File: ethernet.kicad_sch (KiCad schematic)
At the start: 9 parts, among them U1 MX6UL-VM

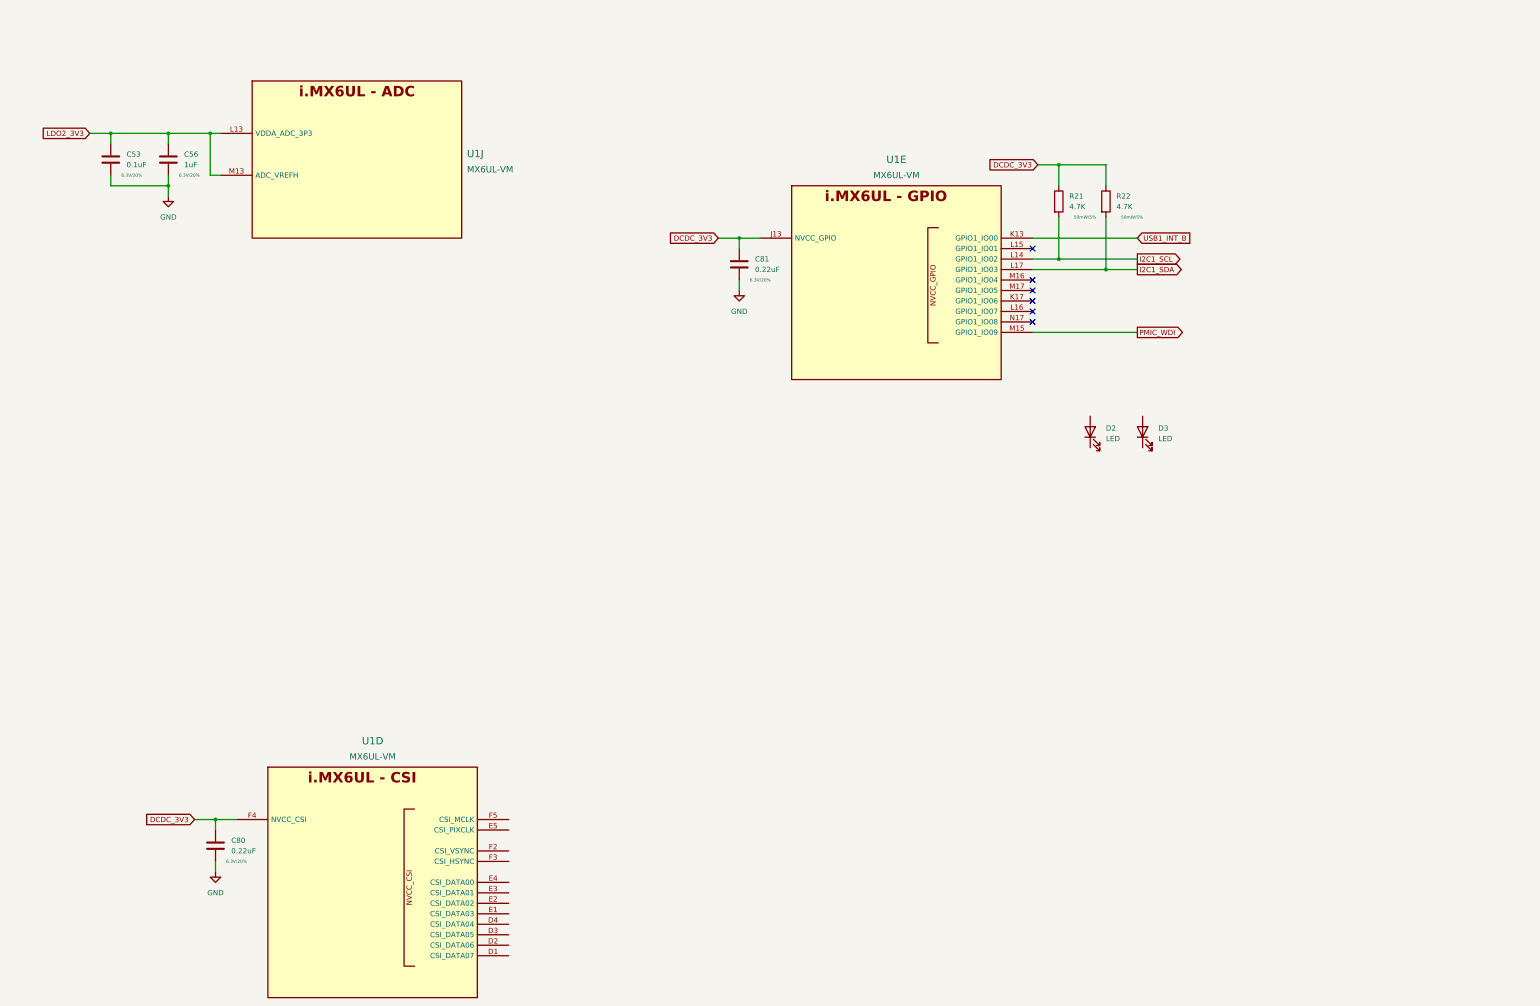
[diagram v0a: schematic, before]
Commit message: more ddr routing, add more connectors
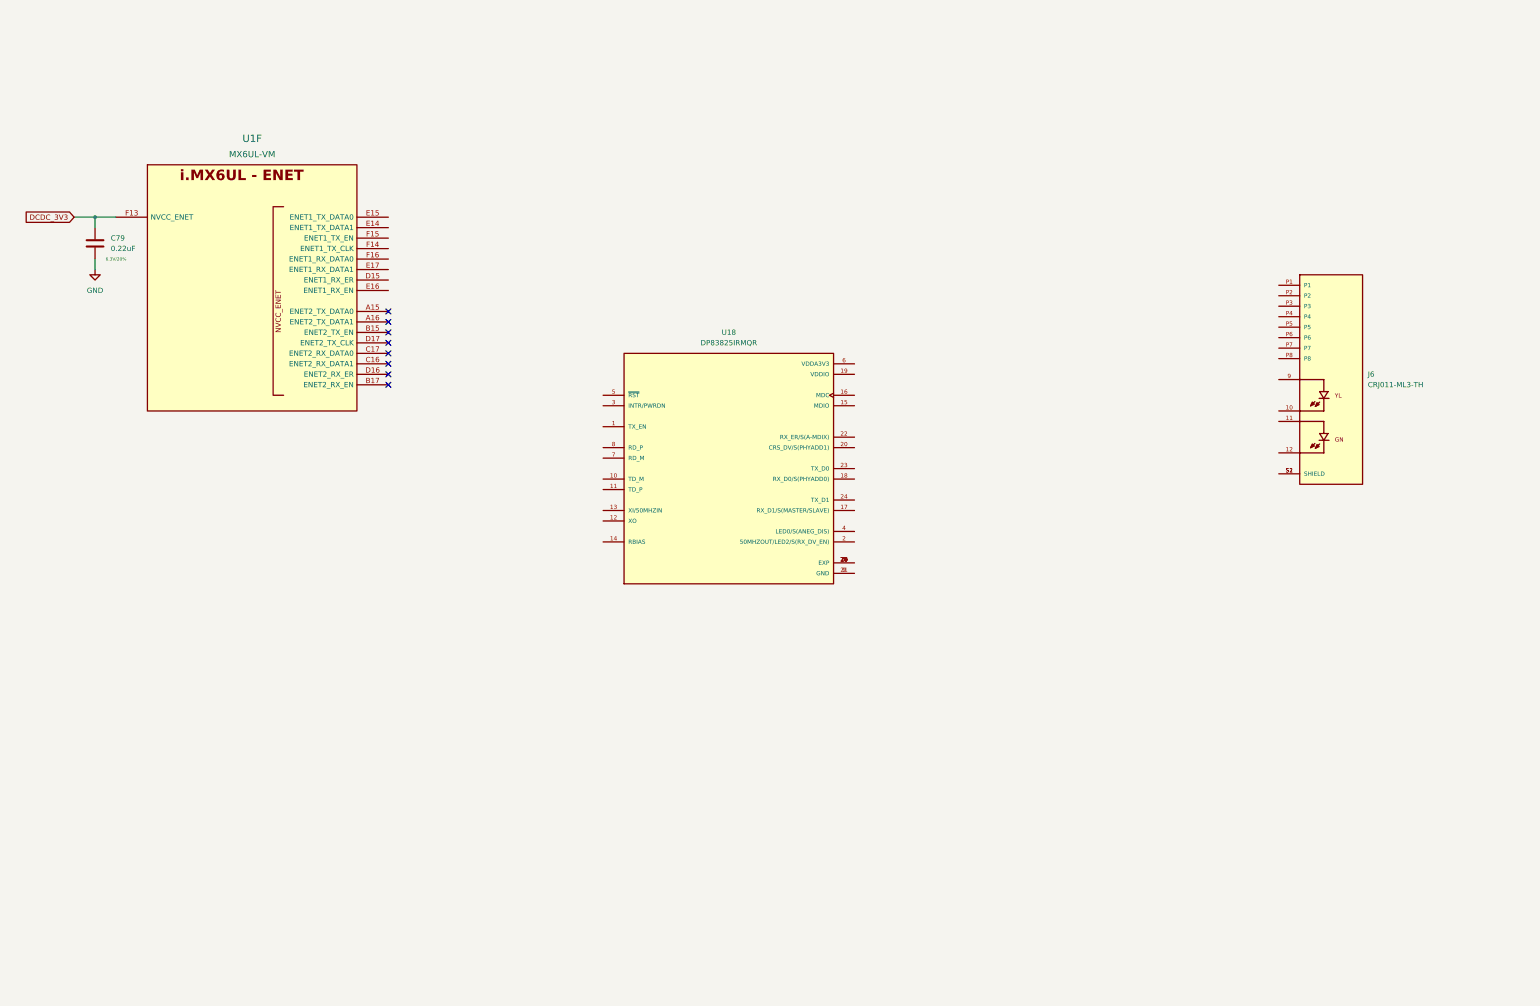
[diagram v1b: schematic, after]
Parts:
- removed C53: 0.1uF, Capacitor_SMD:C_0402_1005Metric, symbol Device:C
- removed C56: 1uF, Capacitor_SMD:C_0402_1005Metric, symbol Device:C
- removed C80, C81: 0.22uF, Capacitor_SMD:C_0402_1005Metric, symbol Device:C
- removed D2, D3: LED, LED_SMD:LED_0603_1608Metric, symbol Device:LED
- removed R21, R22: 4.7K, Resistor_SMD:R_0402_1005Metric, symbol Device:R
- removed U1: MX6UL-VM, imx6ull-sbc:SOT1534-2, symbol imx6ull-sbc:MX6UL-VM
- added C79: 0.22uF, Capacitor_SMD:C_0402_1005Metric, symbol Device:C
- added J6: CRJ011-ML3-TH, imx6ull-sbc:CUI_CRJ011-ML3-TH, symbol imx6ull-sbc:CRJ011-ML3-TH
- added U1: MX6UL-VM, imx6ull-sbc:SOT1534-2, symbol imx6ull-sbc:MX6UL-VM
- added U18: DP83825IRMQR, imx6ull-sbc:XCVR_DP83825IRMQR, symbol imx6ull-sbc:DP83825IRMQR
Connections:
- net DCDC_3V3: now also C79.1, U1.F13 (NVCC_ENET)
- net GND: now also C79.2
- new net: U18.21 (GND), U18.9 (GND)
- new net: U18.25 (EXP), U18.26 (EXP), U18.27 (EXP), U18.28 (EXP), U18.29 (EXP), U18.30 (EXP)
- new net: J6.S1 (SHIELD), J6.S2 (SHIELD)
- no-connect marks 6 -> 8

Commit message: move to hierarchal labels, work on power tree, add basic pcb layout
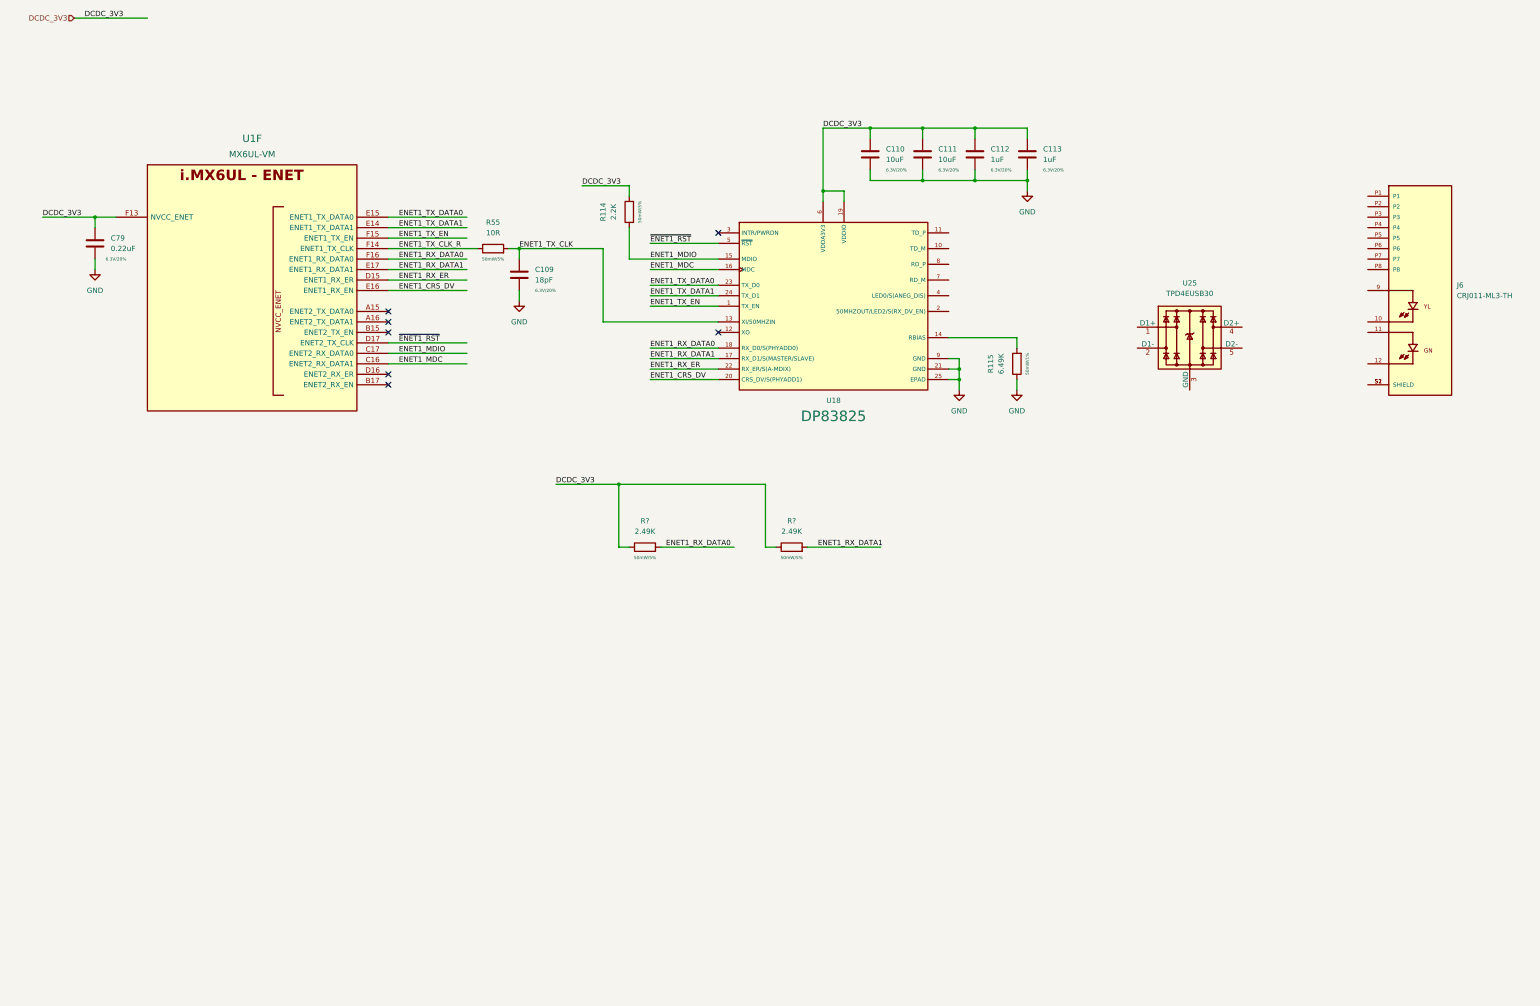
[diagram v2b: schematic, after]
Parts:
- removed U18: DP83825IRMQR, imx6ull-sbc:XCVR_DP83825IRMQR, symbol imx6ull-sbc:DP83825IRMQR
- added C109: 18pF, Capacitor_SMD:C_0402_1005Metric, symbol Device:C
- added C110, C111: 10uF, Capacitor_SMD:C_0402_1005Metric, symbol Device:C
- added C112, C113: 1uF, Capacitor_SMD:C_0402_1005Metric, symbol Device:C
- added R114: 2.2K, Resistor_SMD:R_0402_1005Metric, symbol Device:R
- added R115: 6.49K, Resistor_SMD:R_0402_1005Metric, symbol Device:R
- added R55: 10R, Resistor_SMD:R_0402_1005Metric, symbol Device:R
- added R? (x2): 2.49K, Resistor_SMD:R_0402_1005Metric, symbol Device:R
- added U18: DP83825, imx6ull-sbc:XCVR_DP83825IRMQR, symbol imx6ull-sbc:DP83825
- added U25: TPD4EUSB30, Package_SON:USON-10_2.5x1.0mm_P0.5mm, symbol imx6ull-sbc:TPD4EUSB30
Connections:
- net DCDC_3V3: now also C110.1, C111.1, C112.1, C113.1, R114.2, R?.1, R?.1, U18.19 (VDDIO), U18.6 (VDDA3V3)
- net GND: now also C109.2, C110.2, C111.2, C112.2, C113.2, R115.1, U18.21 (GND), U18.25 (EPAD), U18.9 (GND)
- net ENET1_MDC: now reaches U1.C16 (ENET2_RX_DATA1)
- net ENET1_MDC: now also U18.16 (MDC)
- net ENET1_MDIO: now reaches U1.C17 (ENET2_RX_DATA0)
- net ENET1_MDIO: now also R114.1, U18.15 (MDIO)
- net ENET1_RX_ER: now reaches U1.D15 (ENET1_RX_ER)
- net ENET1_RX_ER: now also U18.22 (RX_ER/S(A-MDIX))
- net ~{ENET1_RST}: now reaches U1.D17 (ENET2_TX_CLK)
- net ~{ENET1_RST}: now also U18.5 (~{RST})
- net ENET1_TX_DATA1: now reaches U1.E14 (ENET1_TX_DATA1)
- net ENET1_TX_DATA1: now also U18.24 (TX_D1)
- net ENET1_TX_DATA0: now reaches U1.E15 (ENET1_TX_DATA0)
- net ENET1_TX_DATA0: now also U18.23 (TX_D0)
- net ENET1_CRS_DV: now reaches U1.E16 (ENET1_RX_EN)
- net ENET1_CRS_DV: now also U18.20 (CRS_DV/S(PHYADD1))
- net ENET1_RX_DATA1: now reaches U1.E17 (ENET1_RX_DATA1)
- net ENET1_RX_DATA1: now also R?.2, U18.17 (RX_D1/S(MASTER/SLAVE))
- net ENET1_TX_CLK_R: now reaches U1.F14 (ENET1_TX_CLK)
- net ENET1_TX_CLK_R: now also R55.1
- net ENET1_TX_EN: now reaches U1.F15 (ENET1_TX_EN)
- net ENET1_TX_EN: now also U18.1 (TX_EN)
- net ENET1_RX_DATA0: now reaches U1.F16 (ENET1_RX_DATA0)
- net ENET1_RX_DATA0: now also R?.2, U18.18 (RX_D0/S(PHYADD0))
- new net: R115.2, U18.14 (RBIAS)
- new net: U25.1 (D1+), U25.10
- new net: U25.2 (D1-), U25.9
- new net: U25.3 (GND), U25.8 (GND)
- new net: U25.4 (D2+), U25.7
- new net: U25.5 (D2-), U25.6
- new net ENET1_TX_CLK: C109.1, R55.2, U18.13 (XI/50MHZIN)
- no-connect marks 8 -> 7
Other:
- moved on the sheet: J6

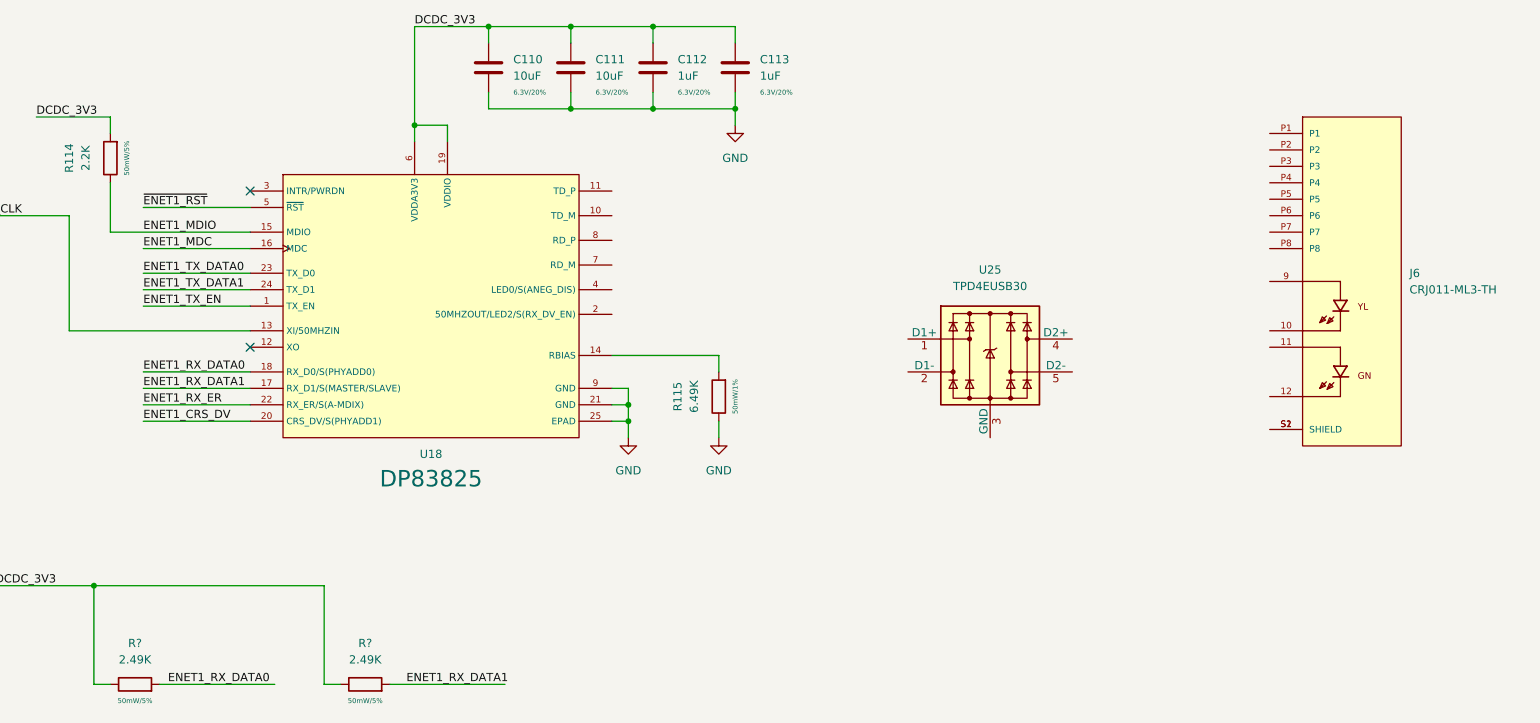
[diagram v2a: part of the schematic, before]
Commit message: most of sch done, inital component pcb placement
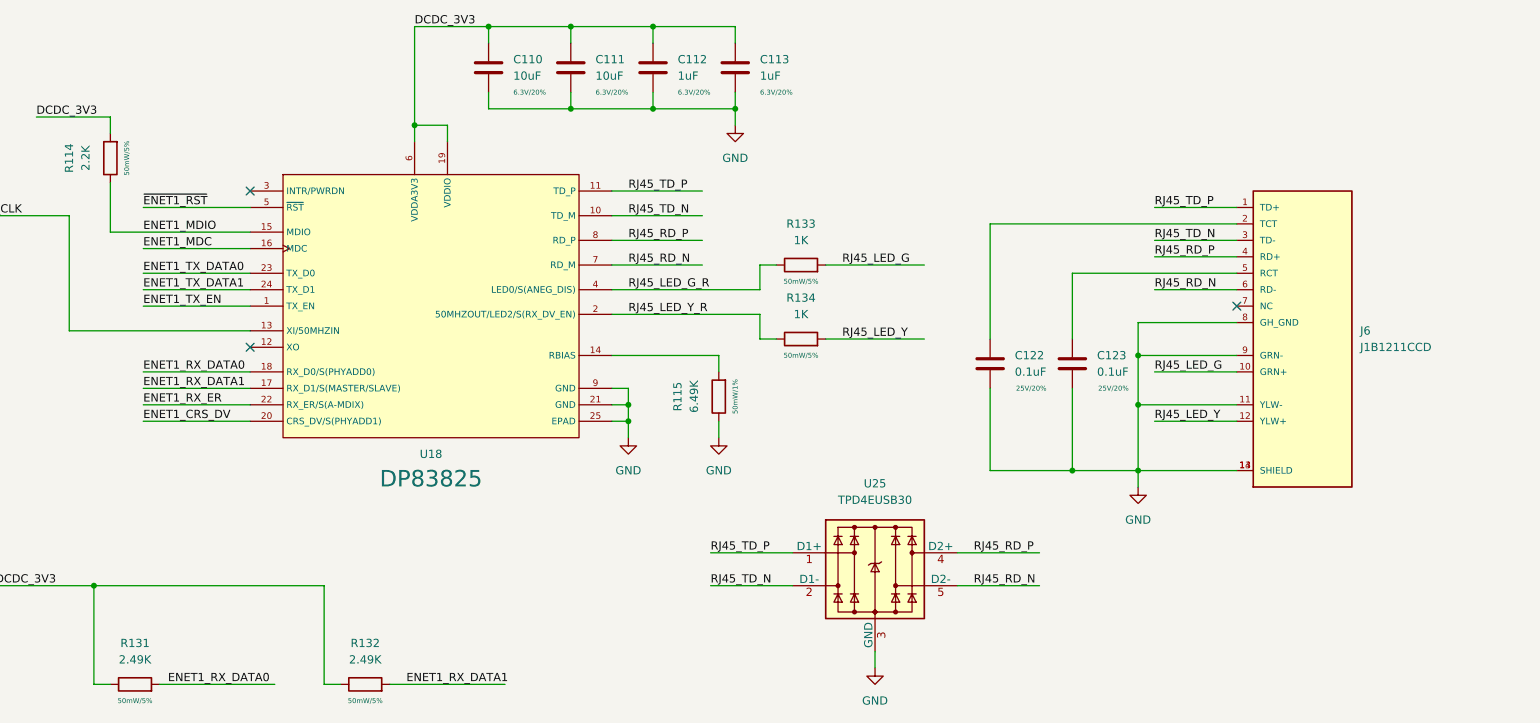
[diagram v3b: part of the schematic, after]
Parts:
- removed J6: CRJ011-ML3-TH, imx6ull-sbc:CUI_CRJ011-ML3-TH, symbol imx6ull-sbc:CRJ011-ML3-TH
- added C122, C123: 0.1uF, Capacitor_SMD:C_0402_1005Metric, symbol Device:C
- added J6: J1B1211CCD, imx6ull-sbc:J1B1211CCD, symbol imx6ull-sbc:J1B1211CCD
- added R133, R134: 1K, Resistor_SMD:R_0402_1005Metric, symbol Device:R
- gave numbers to parts that had none: 2
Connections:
- net GND: now also U25.3 (GND), U25.8 (GND), C122.2, C123.2, J6.11 (YLW-), J6.13 (SHIELD), J6.14 (SHIELD), J6.8 (GH_GND), J6.9 (GRN-)
- net RJ45_TD_N: now reaches U18.10 (TD_M)
- net RJ45_TD_N: now also U25.2 (D1-), U25.9, J6.3 (TD-)
- net RJ45_TD_P: now reaches U18.11 (TD_P)
- net RJ45_TD_P: now also U25.1 (D1+), U25.10, J6.1 (TD+)
- net RJ45_LED_Y_R: now reaches U18.2 (50MHZOUT/LED2/S(RX_DV_EN))
- net RJ45_LED_Y_R: now also R134.1
- net RJ45_LED_G_R: now reaches U18.4 (LED0/S(ANEG_DIS))
- net RJ45_LED_G_R: now also R133.1
- net RJ45_RD_N: now reaches U18.7 (RD_M)
- net RJ45_RD_N: now also U25.5 (D2-), U25.6, J6.6 (RD-)
- net RJ45_RD_P: now reaches U18.8 (RD_P)
- net RJ45_RD_P: now also U25.4 (D2+), U25.7, J6.4 (RD+)
- new net: C122.1, J6.2 (TCT)
- new net: C123.1, J6.5 (RCT)
- new net RJ45_LED_G: J6.10 (GRN+), R133.2
- new net RJ45_LED_Y: J6.12 (YLW+), R134.2
- no-connect marks 7 -> 8
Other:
- moved on the sheet: U25
